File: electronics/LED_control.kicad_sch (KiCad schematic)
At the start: 4 parts, among them J14 Conn_01x03, Q2 IRF6802SD, Q3 IRF6802SD, Q4 IRF6802SD

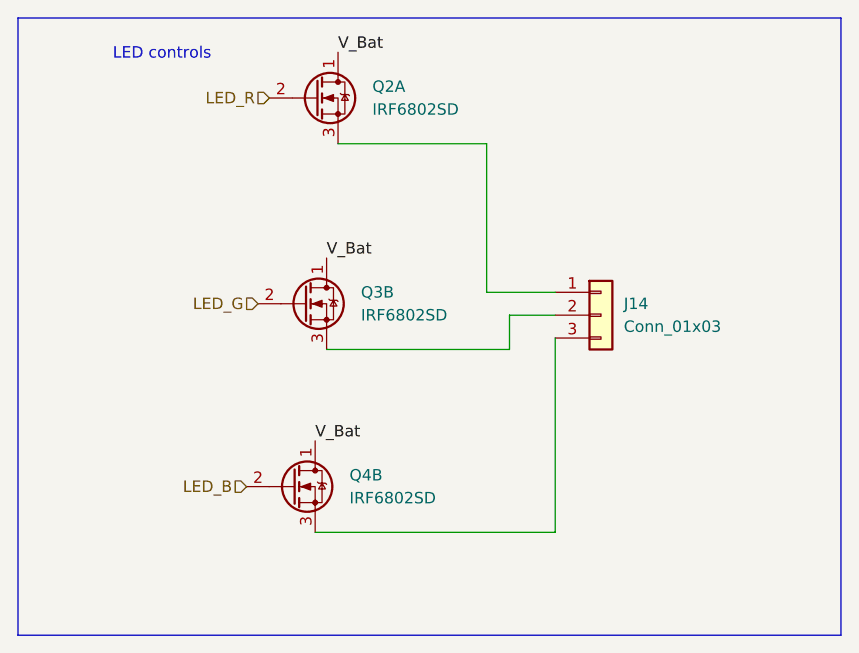
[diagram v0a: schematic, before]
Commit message: LED RGB and temp sensor added
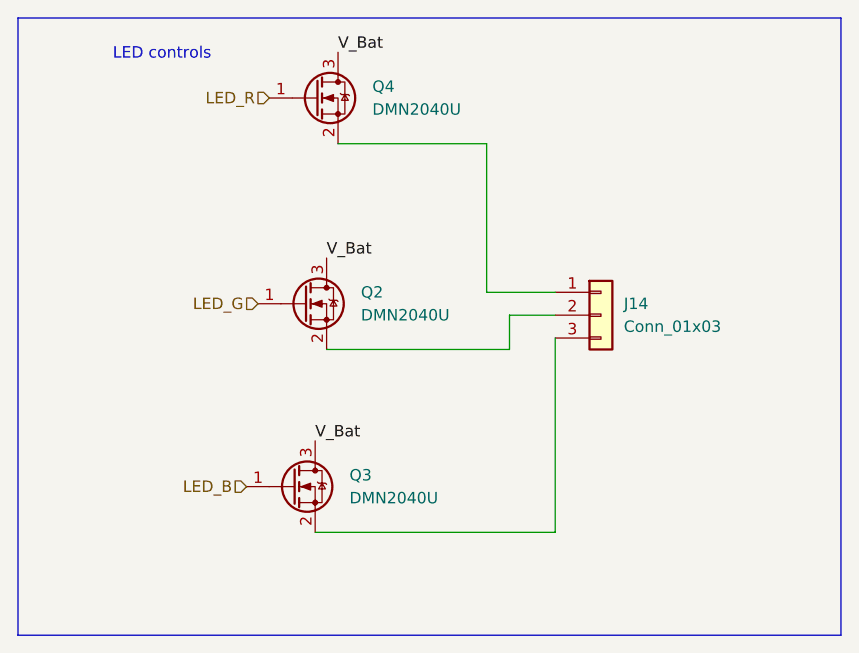
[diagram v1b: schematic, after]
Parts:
- removed Q2, Q3, Q4: IRF6802SD, Package_TO_SOT_SMD:Infineon_PG-HSOF-8-1, symbol Transistor_FET:IRF6802SD
- added Q2, Q3, Q4: DMN2040U, Package_TO_SOT_SMD:SOT-23, symbol Transistor_FET:DMN2040U
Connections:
- net LED_B: now also Q3.1 (G)
- net LED_G: now also Q2.1 (G)
- net LED_R: now also Q4.1 (G)
- net V_Bat: now also Q2.3 (D), Q3.3 (D), Q4.3 (D)
- net at J14.1 (Pin_1): now also Q4.2 (S)
- net at J14.2 (Pin_2): now also Q2.2 (S)
- net at J14.3 (Pin_3): now also Q3.2 (S)
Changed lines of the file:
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@@
 	)
 	(symbol
-		(lib_name "IRF6802SD_1")
-		(lib_id "Transistor_FET:IRF6802SD")
+		(lib_id "Transistor_FET:DMN2040U")
 		(at 69.85 81.28 0)
-		(unit 2)
+		(unit 1)
 		(exclude_from_sim no)
 		(in_bom yes)
@@
 		(dnp no)
 		(fields_autoplaced yes)
-		(property "Reference" "Q3"
+		(property "Reference" "Q2"
 			(at 76.2 80.0099 0)
 			(effects
@@
 			)
 		)
-		(property "Value" "IRF6802SD"
+		(property "Value" "DMN2040U"
 			(at 76.2 82.5499 0)
 			(effects
@@
 			)
 		)
-		(property "Footprint" "Package_TO_SOT_SMD:Infineon_PG-HSOF-8-1"
+		(property "Footprint" "Package_TO_SOT_SMD:SOT-23"
 			(at 74.93 83.185 0)
 			(effects
@@
 			)
 		)
-		(property "Datasheet" "https://www.infineon.com/dgdl/irf6802sdpbf.pdf?fileId=5546d462533600a4015355f0a3021ab2"
+		(property "Datasheet" "https://www.diodes.com/assets/Datasheets/DMN2040U.pdf"
 			(at 74.93 85.09 0)
 			(effects
@@
 			)
 		)
-		(property "Description" "16A Id, 25V Vds, 4.2mOhm Rds, Dual N-Channel MOSFET, DirectFET SA"
-			(at 70.358 93.98 0)
-			(effects
-				(font
-					(size 1.27 1.27)
-				)
-				(hide yes)
-			)
+		(property "Description" "20V Vds, 6A Id, N-Channel MOSFET, SOT-23"
+			(at 69.85 81.28 0)
+			(effects
+				(font
+					(size 1.27 1.27)
+				)
+				(hide yes)
+			)
+		)
+		(pin "1"
 		)
 		(pin "2"
 		)
-		(pin "1"
-		)
 		(pin "3"
-		)
-		(pin "2"
-		)
-		(pin "3"
-		)
-		(pin "1"
 		)
 		(instances
 			(project "electronics"
 				(path "/eeb1234c-eae0-4ac6-a30d-2a978d66d889/04c402f1-b99a-4823-99a0-0c7312782f29/59aad372-c2d2-429c-8a8d-969e1cac44e0"
-					(reference "Q3")
-					(unit 2)
+					(reference "Q2")
+					(unit 1)
 				)
 			)
@@
 	)
 	(symbol
-		(lib_name "IRF6802SD_2")
-		(lib_id "Transistor_FET:IRF6802SD")
-		(at 68.58 101.6 0)
-		(unit 2)
-		(exclude_from_sim no)
-		(in_bom yes)
-		(on_board yes)
-		(dnp no)
-		(fields_autoplaced yes)
-		(property "Reference" "Q4"
-			(at 74.93 100.3299 0)
-			(effects
-				(font
-					(size 1.27 1.27)
-				)
-				(justify left)
-			)
-		)
-		(property "Value" "IRF6802SD"
-			(at 74.93 102.8699 0)
-			(effects
-				(font
-					(size 1.27 1.27)
-				)
-				(justify left)
-			)
-		)
-		(property "Footprint" "Package_TO_SOT_SMD:Infineon_PG-HSOF-8-1"
-			(at 73.66 103.505 0)
-			(effects
-				(font
-					(size 1.27 1.27)
-					(italic yes)
-				)
-				(justify left)
-				(hide yes)
-			)
-		)
-		(property "Datasheet" "https://www.infineon.com/dgdl/irf6802sdpbf.pdf?fileId=5546d462533600a4015355f0a3021ab2"
-			(at 73.66 105.41 0)
-			(effects
-				(font
-					(size 1.27 1.27)
-				)
-				(justify left)
-				(hide yes)
-			)
-		)
-		(property "Description" "16A Id, 25V Vds, 4.2mOhm Rds, Dual N-Channel MOSFET, DirectFET SA"
-			(at 69.088 114.3 0)
-			(effects
-				(font
-					(size 1.27 1.27)
-				)
-				(hide yes)
-			)
-		)
-		(pin "2"
-		)
-		(pin "1"
-		)
-		(pin "3"
-		)
-		(pin "2"
-		)
-		(pin "3"
-		)
-		(pin "1"
-		)
-		(instances
-			(project "electronics"
-				(path "/eeb1234c-eae0-4ac6-a30d-2a978d66d889/04c402f1-b99a-4823-99a0-0c7312782f29/59aad372-c2d2-429c-8a8d-969e1cac44e0"
-					(reference "Q4")
-					(unit 2)
-				)
-			)
-		)
-	)
-	(symbol
-		(lib_id "Transistor_FET:IRF6802SD")
+		(lib_id "Transistor_FET:DMN2040U")
 		(at 71.12 58.42 0)
 		(unit 1)
@@
 		(dnp no)
 		(fields_autoplaced yes)
-		(property "Reference" "Q2"
+		(property "Reference" "Q4"
 			(at 77.47 57.1499 0)
 			(effects
@@
 			)
 		)
-		(property "Value" "IRF6802SD"
+		(property "Value" "DMN2040U"
 			(at 77.47 59.6899 0)
 			(effects
@@
 			)
 		)
-		(property "Footprint" "Package_TO_SOT_SMD:Infineon_PG-HSOF-8-1"
+		(property "Footprint" "Package_TO_SOT_SMD:SOT-23"
 			(at 76.2 60.325 0)
 			(effects
@@
 			)
 		)
-		(property "Datasheet" "https://www.infineon.com/dgdl/irf6802sdpbf.pdf?fileId=5546d462533600a4015355f0a3021ab2"
+		(property "Datasheet" "https://www.diodes.com/assets/Datasheets/DMN2040U.pdf"
 			(at 76.2 62.23 0)
 			(effects
@@
 			)
 		)
-		(property "Description" "16A Id, 25V Vds, 4.2mOhm Rds, Dual N-Channel MOSFET, DirectFET SA"
-			(at 71.628 71.12 0)
-			(effects
-				(font
-					(size 1.27 1.27)
-				)
-				(hide yes)
-			)
+		(property "Description" "20V Vds, 6A Id, N-Channel MOSFET, SOT-23"
+			(at 71.12 58.42 0)
+			(effects
+				(font
+					(size 1.27 1.27)
+				)
+				(hide yes)
+			)
+		)
+		(pin "1"
 		)
 		(pin "2"
 		)
+		(pin "3"
+		)
+		(instances
+			(project ""
+				(path "/eeb1234c-eae0-4ac6-a30d-2a978d66d889/04c402f1-b99a-4823-99a0-0c7312782f29/59aad372-c2d2-429c-8a8d-969e1cac44e0"
+					(reference "Q4")
+					(unit 1)
+				)
+			)
+		)
+	)
+	(symbol
+		(lib_id "Transistor_FET:DMN2040U")
+		(at 68.58 101.6 0)
+		(unit 1)
+		(exclude_from_sim no)
+		(in_bom yes)
+		(on_board yes)
+		(dnp no)
+		(fields_autoplaced yes)
+		(property "Reference" "Q3"
+			(at 74.93 100.3299 0)
+			(effects
+				(font
+					(size 1.27 1.27)
+				)
+				(justify left)
+			)
+		)
+		(property "Value" "DMN2040U"
+			(at 74.93 102.8699 0)
+			(effects
+				(font
+					(size 1.27 1.27)
+				)
+				(justify left)
+			)
+		)
+		(property "Footprint" "Package_TO_SOT_SMD:SOT-23"
+			(at 73.66 103.505 0)
+			(effects
+				(font
+					(size 1.27 1.27)
+					(italic yes)
+				)
+				(justify left)
+				(hide yes)
+			)
+		)
+		(property "Datasheet" "https://www.diodes.com/assets/Datasheets/DMN2040U.pdf"
+			(at 73.66 105.41 0)
+			(effects
+				(font
+					(size 1.27 1.27)
+				)
+				(justify left)
+				(hide yes)
+			)
+		)
+		(property "Description" "20V Vds, 6A Id, N-Channel MOSFET, SOT-23"
+			(at 68.58 101.6 0)
+			(effects
+				(font
+					(size 1.27 1.27)
+				)
+				(hide yes)
+			)
+		)
 		(pin "1"
 		)
-		(pin "4"
-		)
-		(pin "5"
+		(pin "2"
 		)
 		(pin "3"
-		)
-		(pin "1"
 		)
 		(instances
 			(project "electronics"
 				(path "/eeb1234c-eae0-4ac6-a30d-2a978d66d889/04c402f1-b99a-4823-99a0-0c7312782f29/59aad372-c2d2-429c-8a8d-969e1cac44e0"
-					(reference "Q2")
+					(reference "Q3")
 					(unit 1)
 				)
